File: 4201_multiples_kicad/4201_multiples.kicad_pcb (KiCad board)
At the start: 2 copper layers, 60 x 110 mm, 73 parts, among them J1 AudioJack2, J10 Conn_01x04_Female, J11 Conn_01x05_Female, J12 Conn_01x04_Female, J13 Conn_01x04_Female, J14 Conn_01x05_Male, J15 Conn_01x04_Male, J16 Conn_01x05_Male, J17 Conn_01x04_Male, J18 Conn_01x04_Male, J19 Conn_02x05_Odd_Even, J2 AudioJack2, J3 AudioJack2, J4 AudioJack2, J5 AudioJack2, J6 AudioJack2, J7 AudioJack2, J8 AudioJack2, J9 Conn_01x05_Female, U1 TL074, U2 TL074

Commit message: Small touches
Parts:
- D13, D14: value 1N5817 -> Schottky
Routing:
- net /interface/LED_2N_K: track 31.5 -> 30.7 mm
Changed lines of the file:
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@@
       (effects (font (size 1 1) (thickness 0.15)) (justify mirror))
     )
-    (fp_text value "1N5817" (at 0 -1.82) (layer "B.Fab") hide
+    (fp_text value "Schottky" (at 0 -1.82) (layer "B.Fab") hide
       (effects (font (size 1 1) (thickness 0.15)) (justify mirror))
     )
@@
       (effects (font (size 1 1) (thickness 0.15)) (justify mirror))
     )
-    (fp_text value "1N5817" (at 0 -1.82) (layer "B.Fab") hide
+    (fp_text value "Schottky" (at 0 -1.82) (layer "B.Fab") hide
       (effects (font (size 1 1) (thickness 0.15)) (justify mirror))
     )
@@
   (segment (start 95.885 67.31) (end 95.885 60.325) (width 0.2) (layer "F.Cu") (net 5))
   (segment (start 97.16 59.05) (end 97.16 55.88) (width 0.2) (layer "F.Cu") (net 5))
-  (segment (start 99.949 140.716) (end 99.949 108.331) (width 0.2) (layer "F.Cu") (net 6))
-  (segment (start 98.425 142.24) (end 99.949 140.716) (width 0.2) (layer "F.Cu") (net 6))
+  (segment (start 98.298 142.24) (end 99.568 140.97) (width 0.2) (layer "F.Cu") (net 6))
+  (segment (start 99.568 107.95) (end 98.298 106.68) (width 0.2) (layer "F.Cu") (net 6))
+  (segment (start 99.568 140.97) (end 99.568 107.95) (width 0.2) (layer "F.Cu") (net 6))
   (segment (start 98.298 106.68) (end 97.15 106.68) (width 0.2) (layer "F.Cu") (net 6))
-  (segment (start 97.155 142.24) (end 98.425 142.24) (width 0.2) (layer "F.Cu") (net 6))
-  (segment (start 99.949 108.331) (end 98.298 106.68) (width 0.2) (layer "F.Cu") (net 6))
-  (segment (start 97.155 139.7) (end 98.425 139.7) (width 0.2) (layer "F.Cu") (net 7))
-  (segment (start 99.06 119.38) (end 97.155 117.475) (width 0.2) (layer "F.Cu") (net 7))
-  (segment (start 98.425 139.7) (end 99.06 139.065) (width 0.2) (layer "F.Cu") (net 7))
-  (segment (start 99.06 139.065) (end 99.06 119.38) (width 0.2) (layer "F.Cu") (net 7))
+  (segment (start 97.155 142.24) (end 98.298 142.24) (width 0.2) (layer "F.Cu") (net 6))
+  (segment (start 98.552 118.872) (end 97.155 117.475) (width 0.2) (layer "F.Cu") (net 7))
+  (segment (start 98.552 138.938) (end 98.552 118.872) (width 0.2) (layer "F.Cu") (net 7))
   (segment (start 97.155 117.475) (end 97.155 110.49) (width 0.2) (layer "F.Cu") (net 7))
+  (segment (start 97.79 139.7) (end 98.552 138.938) (width 0.2) (layer "F.Cu") (net 7))
+  (segment (start 97.155 139.7) (end 97.79 139.7) (width 0.2) (layer "F.Cu") (net 7))
   (segment (start 133.8215 63.246) (end 134.874 63.246) (width 0.2) (layer "B.Cu") (net 8))
   (segment (start 135.636 64.008) (end 135.636 65.786) (width 0.2) (layer "B.Cu") (net 8))

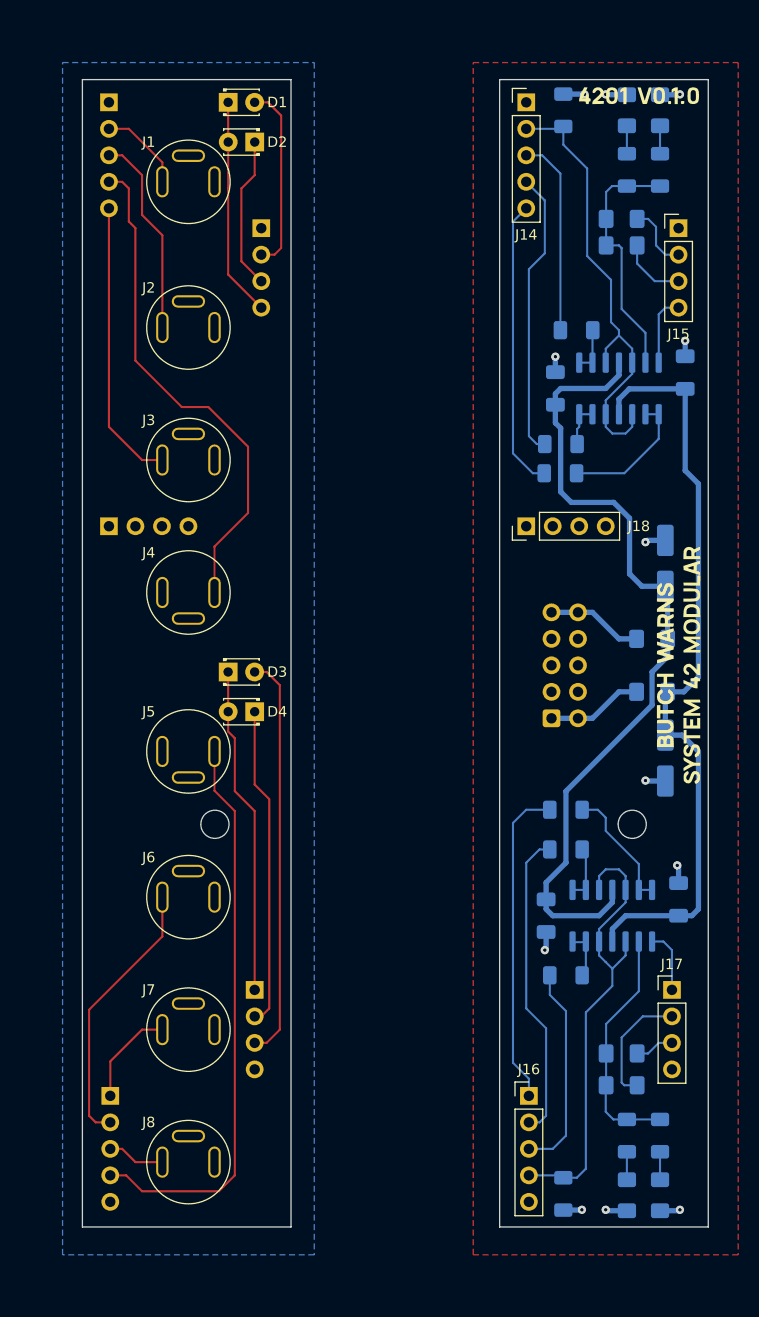
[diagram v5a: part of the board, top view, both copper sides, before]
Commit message: Add stitching vias and clean up files
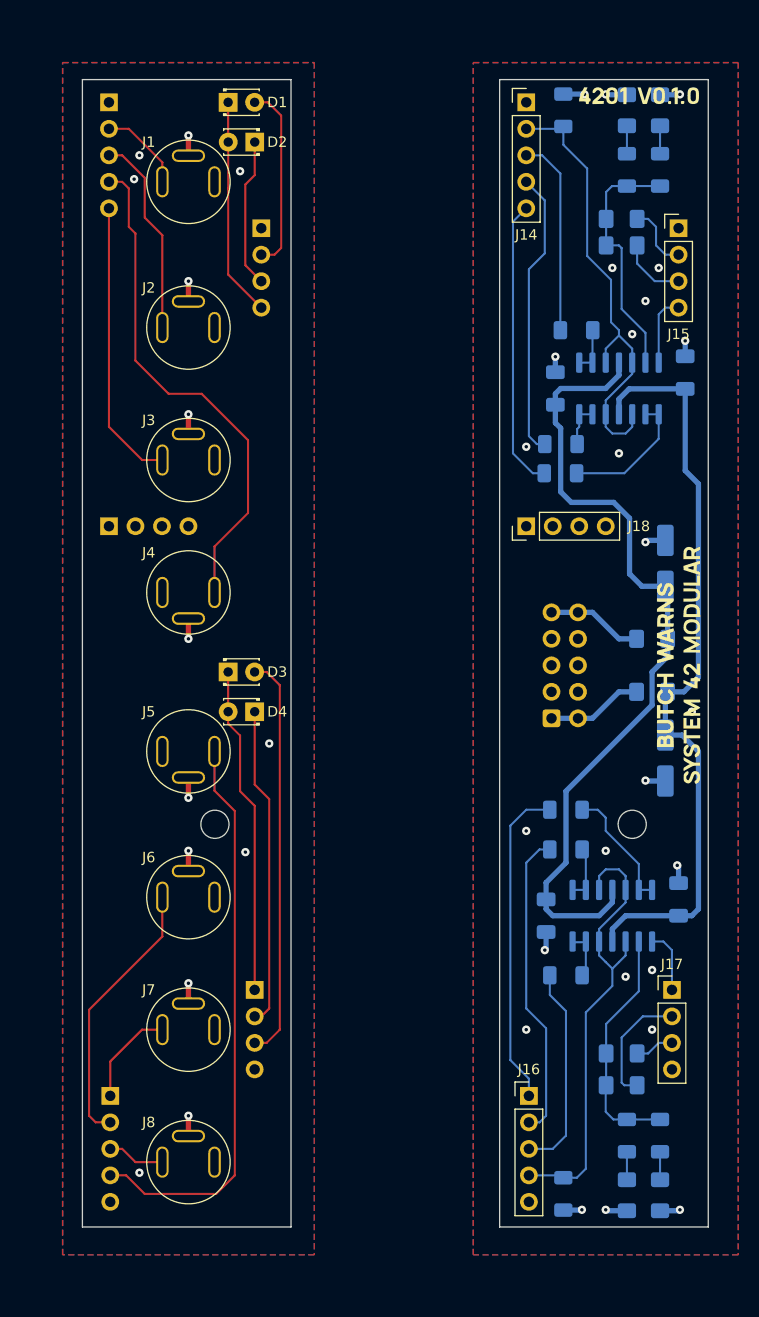
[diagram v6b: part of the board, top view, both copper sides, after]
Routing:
- net /interface/0V: track 0.00 -> 15.5 mm, vias 0 -> 14
- net GND: vias 12 -> 25
- added copper zone on F.Cu, net /interface/0V

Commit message: Small changes, cleanup
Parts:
- removed the G*** at (52.9, 42.1)
- added G***: LOGO, 4201_multiples:4201_panel_silk, F.Cu at (52.9, 42.1)
- added G***: LOGO, 4201_multiples:2022, F.Cu at (137.2, 158.1)
- D1, D3: value 1.8mm_green -> 1.8mm_red
- D2: value 1.8mm_red -> 1.8mm_green
- D4: value 1.8mm_red -> green
- J1, J2, J3, J4, J5, J6, J7, J8: value AudioJack2 -> PJ392
- R2, R8: value 39k -> 4k7
- R3, R9: value 4k7 -> 39k
- moved D3 4.58 mm to (97.2, 110.5), turned to 180 degrees
- moved D4 3.81 mm to (97.2, 106.7)
- moved D1 3.81 mm to (94.6, 55.9)
- moved D2 3.81 mm to (97.2, 52.1)
- moved D8 3.47 mm to (132.6, 53.3)
- moved D11 3.45 mm to (132.6, 156.5)
- moved D7 2.84 mm to (135.6, 53.3)
- moved D12 2.82 mm to (135.6, 156.5)
- moved C6 0.67 mm to (138.4, 128.3)
- moved R4 0.57 mm to (128.5, 73.7)
- moved R2 0.57 mm to (132.6, 59.1)
- moved R3 0.54 mm to (135.6, 58.9)
- moved R8 0.46 mm to (135.6, 150.9)
- moved R9 0.36 mm to (132.6, 150.9)
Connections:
- net /interface/LED_1N_K renamed /interface/LED_1P_K
- net /interface/LED_1P_A renamed /interface/LED_1N_A
- net /interface/LED_1_PK_NA renamed /interface/LED_1_PA_NK
- net /interface/LED_2N_K renamed /interface/LED_2P_K
- net /interface/LED_2P_A renamed /interface/LED_2N_A
- net /interface/LED_2_PK_NA renamed /interface/LED_2_PA_NK
- net /main_board/LED_1N_K renamed /main_board/LED_1P_K
- net /main_board/LED_1P_A renamed /main_board/LED_1N_A
- net /main_board/LED_1_PK_NA renamed /main_board/LED_1_PA_NK
- net /main_board/LED_2N_K renamed /main_board/LED_2P_K
- net /main_board/LED_2P_A renamed /main_board/LED_2N_A
- net /main_board/LED_2_PK_NA renamed /main_board/LED_2_PN_KA
- D7 pad 2: Net-(D7-Pad2) -> Net-(R3-Pad2)
- R2 pad 2: Net-(D7-Pad2) -> Net-(D8-Pad1)
- R3 pad 2: Net-(D8-Pad1) -> Net-(R3-Pad2)
- R8 pad 2: Net-(D11-Pad2) -> Net-(D12-Pad1)
- R9 pad 2: Net-(D12-Pad1) -> Net-(D11-Pad2)
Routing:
- net /interface/LED_1N_A: track 17.9 -> 12.9 mm
- net /interface/LED_2N_A: track 38.9 -> 33.9 mm
- net /interface/LED_1P_K: track 14.3 -> 18.5 mm
- net /interface/LED_2P_K: track 30.7 -> 34.6 mm
- net Net-(D7-Pad2): track 2.68 -> 0.00 mm
- net Net-(R3-Pad2): track 0.00 -> 2.55 mm
- net Net-(D6-Pad1): track 24.1 -> 22.5 mm
- net Net-(R9-Pad1): track 23.1 -> 21.9 mm
- net -12V: track 73.3 -> 72.1 mm
- net /main_board/OUT_1_3: track 27.6 -> 26.4 mm
- net /interface/OUT_2_1: track 26.0 -> 25.1 mm
- net /interface/LED_2_PA_NK: track 31.5 -> 32.1 mm
- net /main_board/OUT_1_2: track 27.8 -> 27.3 mm
- net GND: track 22.2 -> 22.4 mm, vias 25 -> 28
- net /interface/0V: vias 14 -> 16

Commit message: Fix panel copper
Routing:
- added copper zone on B.Cu, net (none)
- added copper zone on F.Cu, net (none)
